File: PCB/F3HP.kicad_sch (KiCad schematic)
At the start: 108 parts, among them J1 L_In, J2 R_In, J3 AC_In, J4 Switch, J5 HPOut, K1 C93402, Q1 BC850C, Q10 BC860C, Q2 BC860C, Q3 BCP56, Q4 BC850C, Q5 BC860C, Q6 BCP56, Q7 BC850C, Q8 AO3400A, Q9 BC860C, U1 LT1965

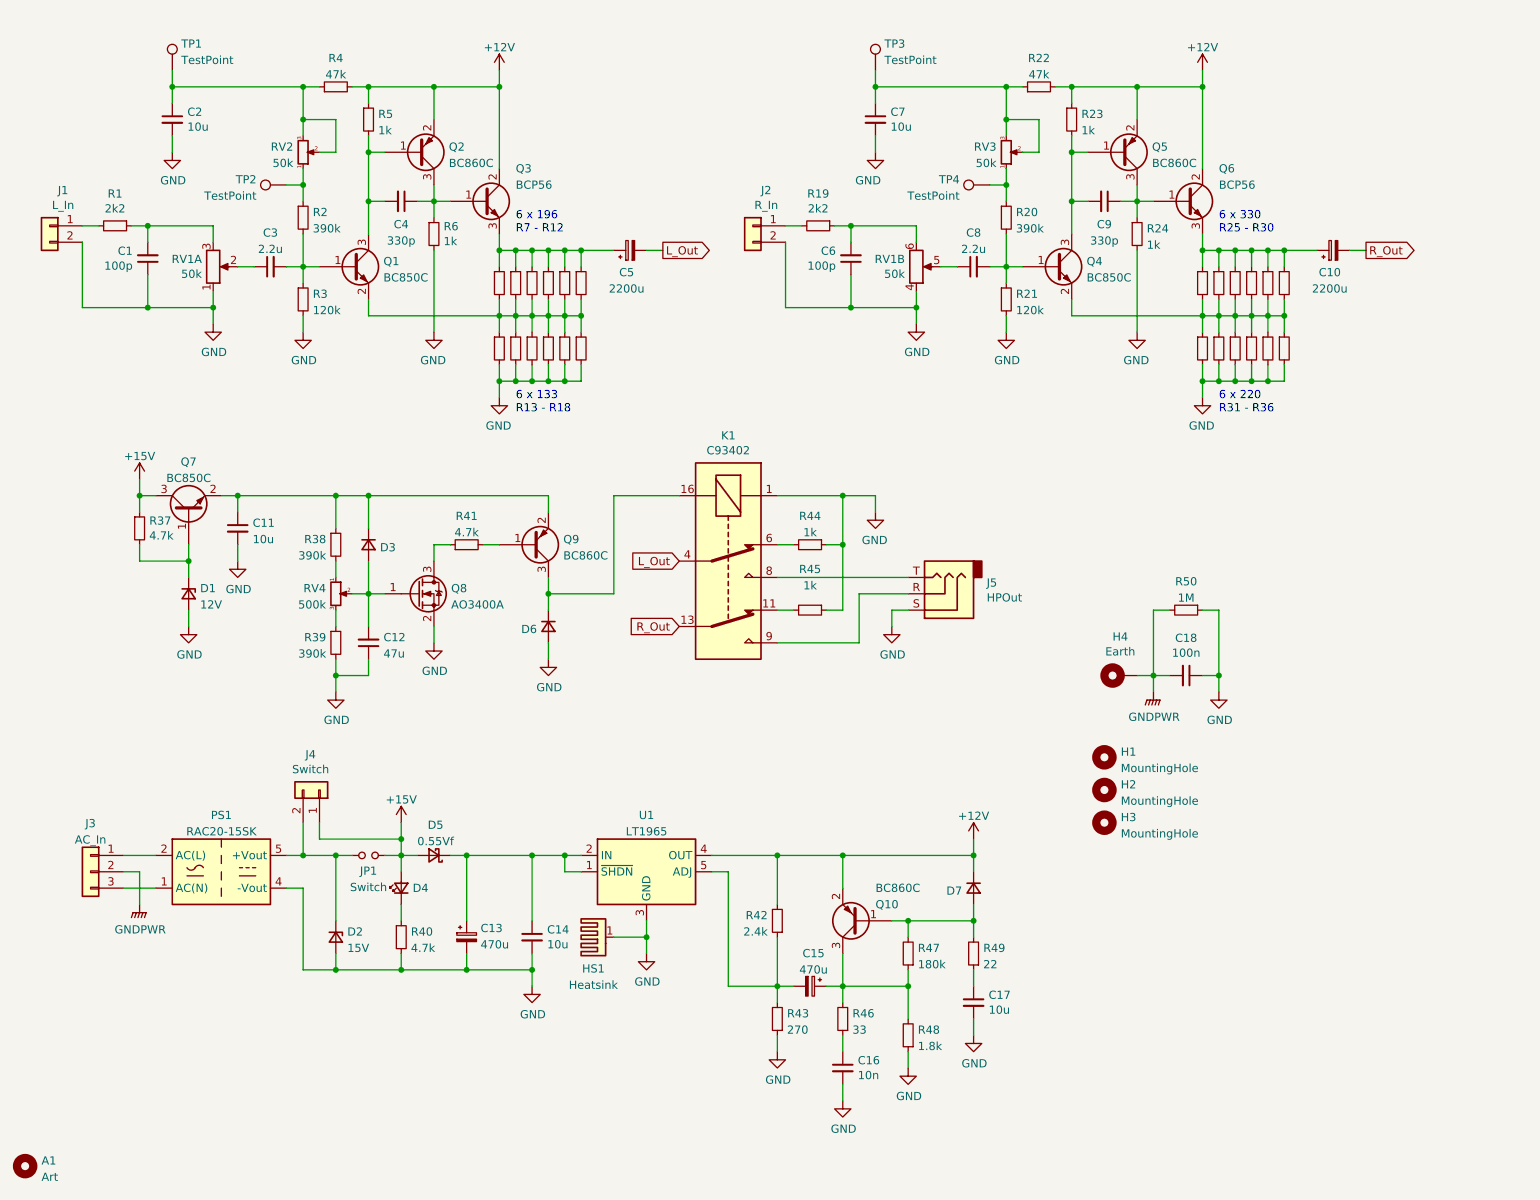
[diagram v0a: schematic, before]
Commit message: Better layout, better heatsinking
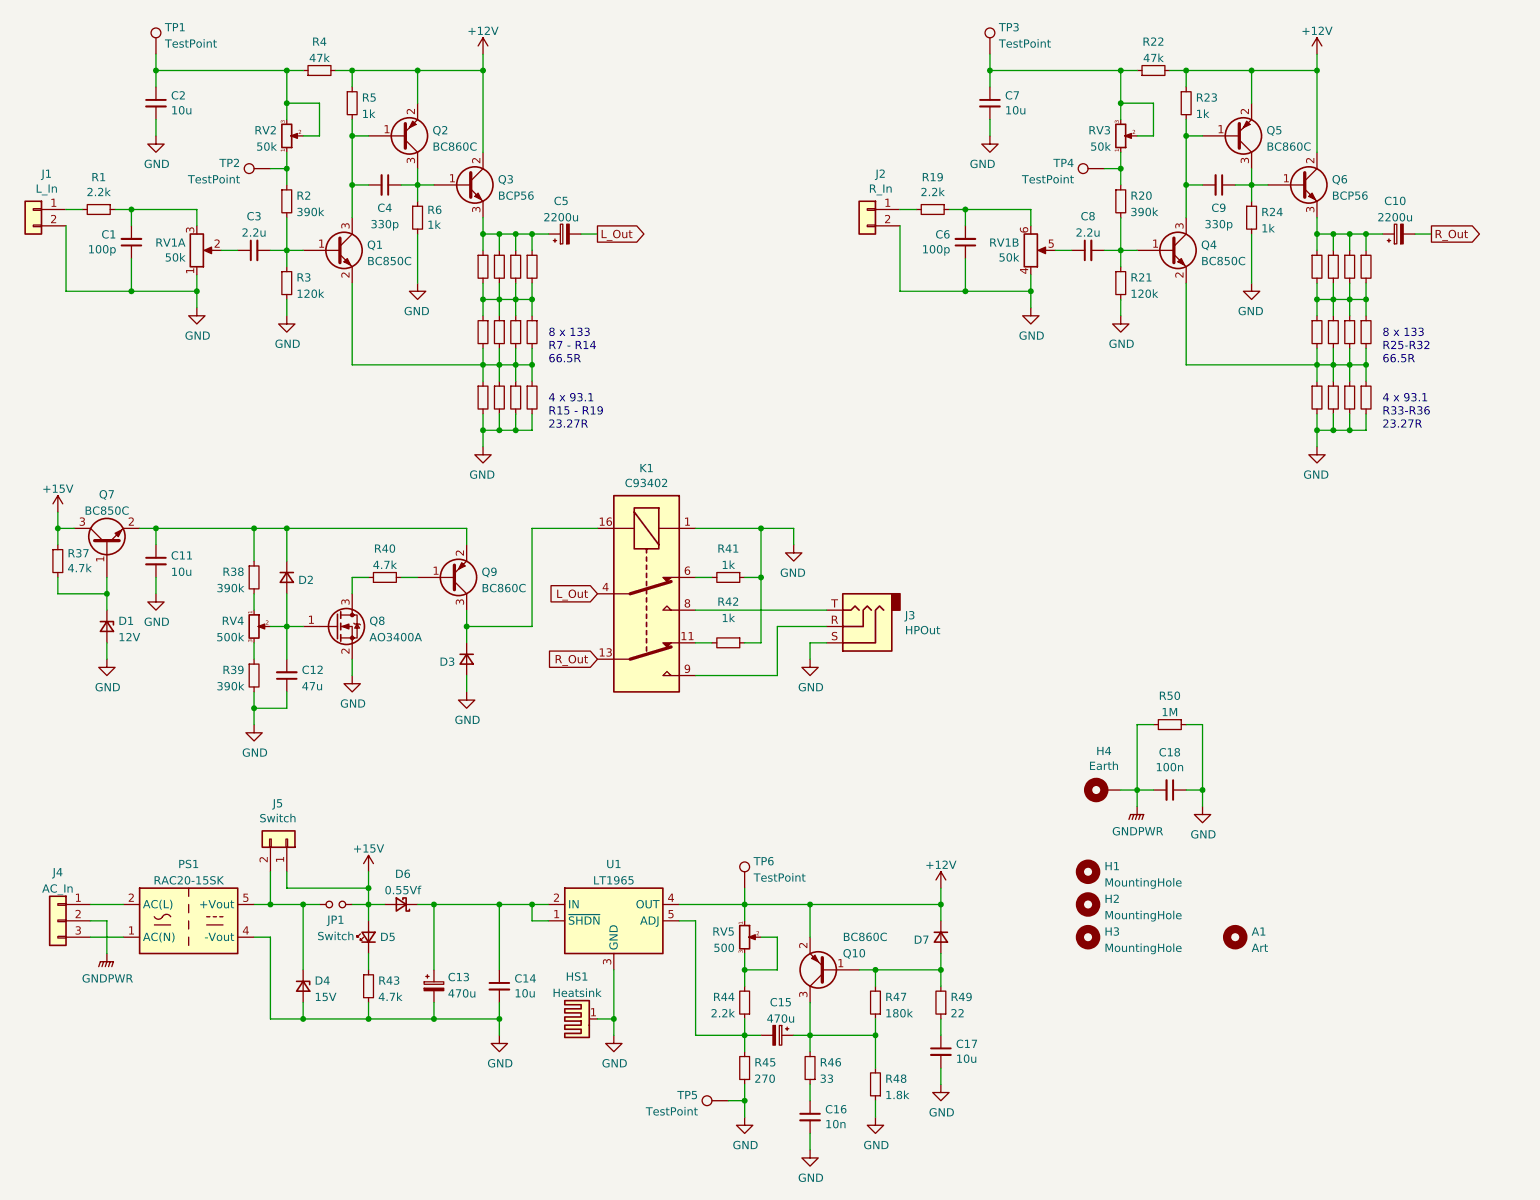
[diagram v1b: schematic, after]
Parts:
- removed R16, R17, R34, R35: 133, Resistor_SMD:R_1206_3216Metric, symbol Device:R_Small
- added R13, R14, R31, R32: 133, Resistor_SMD:R_1206_3216Metric, symbol Device:R_Small
- added RV5: 500, Potentiometer_THT:Potentiometer_Vishay_T73YP_Vertical, symbol Device:R_Potentiometer_Small
- added TP5, TP6: TestPoint, TestPoint:TestPoint_THTPad_D1.5mm_Drill0.7mm, symbol Connector:TestPoint
- Q3, Q6: LCSC part number C177012 -> (none); Part number BCP56TA -> (none)
- R1, R19: value 2k2 -> 2.2k
- R10: renamed from R11; value 196 -> 133; Part number RT1206FRE07196RL -> RT1206DRD07133RL
- R11: renamed from R9; value 196 -> 133; Part number RT1206FRE07196RL -> RT1206DRD07133RL
- R12, R25, R30, R7: value 196 -> 133; Part number RT1206FRE07196RL -> RT1206DRD07133RL
- R15: renamed from R13; value 133 -> 93.1; Part number RT1206DRD07133RL -> RT1206FRE0793R1L
- R16: renamed from R14; value 133 -> 93.1; Part number RT1206DRD07133RL -> RT1206FRE0793R1L
- R17: renamed from R15; value 133 -> 93.1; Part number RT1206DRD07133RL -> RT1206FRE0793R1L
- R18, R36: value 133 -> 93.1; Part number RT1206DRD07133RL -> RT1206FRE0793R1L
- R26: renamed from R28; value 196 -> 133; Part number RT1206FRE07196RL -> RT1206DRD07133RL
- R27: renamed from R26; value 196 -> 133; Part number RT1206FRE07196RL -> RT1206DRD07133RL
- R28: renamed from R29; value 196 -> 133; Part number RT1206FRE07196RL -> RT1206DRD07133RL
- R29: renamed from R27; value 196 -> 133; Part number RT1206FRE07196RL -> RT1206DRD07133RL
- R33: renamed from R31; value 133 -> 93.1; Part number RT1206DRD07133RL -> RT1206FRE0793R1L
- R34: renamed from R32; value 133 -> 93.1; Part number RT1206DRD07133RL -> RT1206FRE0793R1L
- R35: renamed from R33; value 133 -> 93.1; Part number RT1206DRD07133RL -> RT1206FRE0793R1L
- R44: renamed from R42; value 2.4k -> 2.2k; LCSC part number C784582 -> C706068; Part number RT0603BRE072K4L -> RT0603DRE072K2L
- R8: renamed from R10; value 196 -> 133; Part number RT1206FRE07196RL -> RT1206DRD07133RL
- R9: renamed from R8; value 196 -> 133; Part number RT1206FRE07196RL -> RT1206DRD07133RL
- RV2, RV3: LCSC part number C83686 -> C780226; Part number 3296W-1-503LF -> 3266W-1-503LF
- renumbered D3 to D2, D6 to D3, D2 to D4, D4 to D5, D5 to D6, J5 to J3, J3 to J4, J4 to J5, R41 to R40, R44 to R41, R45 to R42, R40 to R43, R43 to R45
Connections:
- net +12V: now also RV5.1, TP6.1; no longer R44.2
- net GND: now also TP5.1
- net at C5.1, Q3.3 (E), R11.1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: now also R13.1; no longer R10.1, R12.1, R8.1
- net at Q1.2 (E), R10.2, R12.2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: now also R14.2; no longer R11.2, R7.2, R9.2
- net at Q4.2 (E), R26.2, R28.2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: now also R32.2; no longer R25.2, R27.2, R29.2
- net at C10.1, Q6.3 (E), R25.1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: now also R31.1; no longer R26.1, R28.1, R30.1
- new net: R10.1, R11.2, R12.1, R13.2, R14.1, R7.2, R8.1, R9.2
- new net: R25.2, R26.1, R27.2, R28.1, R29.2, R30.1, R31.2, R32.1
- new net: R44.2, RV5.2, RV5.3
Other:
- note added: "4 x 93.1 R15 - R19 23.27R"
- note added: "4 x 93.1 R33-R36 23.27R"
- note added: "8 x 133 R25-R32 66.5R"
- note added: "8 x 133 R7 - R14 66.5R"
- note removed: "6 x 133 R13 - R18"
- note removed: "6 x 196 R7 - R12"
- note removed: "6 x 220 R31 - R36"
- note removed: "6 x 330 R25 - R30"
- moved on the sheet: C1, C10, C11, C12, C13, C14, C15, C16, C17, C18, C2, C3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

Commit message: Updated component values and BOM
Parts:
- HS1: LCSC part number (none) -> N/A; Part number (none) -> 573300D00000G
- Q1, Q4, Q7: Part number BC850C,235 -> BC850C
- Q10, Q2, Q5, Q9: Part number BC860C,235 -> BC860C
- Q3, Q6: value BCP56 -> BCP56TA; LCSC part number (none) -> C177012; Part number (none) -> BCP56TA
- R22, R4: value 47k -> 39k; LCSC part number C326743 -> C705983; Part number RT0603BRE0747KL -> RT0603DRD0739RL
- R23, R5: value 1k -> 820; LCSC part number C706049 -> C723589; Part number RT0603DRE071KL -> RT0603DRD07820RL
- R24, R6: value 1k -> 1.2k; LCSC part number C706049 -> C723656; Part number RT0603DRE071KL -> RT0603DRD071K2L
- RV2, RV3: value 50k -> 5k
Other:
- moved on the sheet: C10, C5

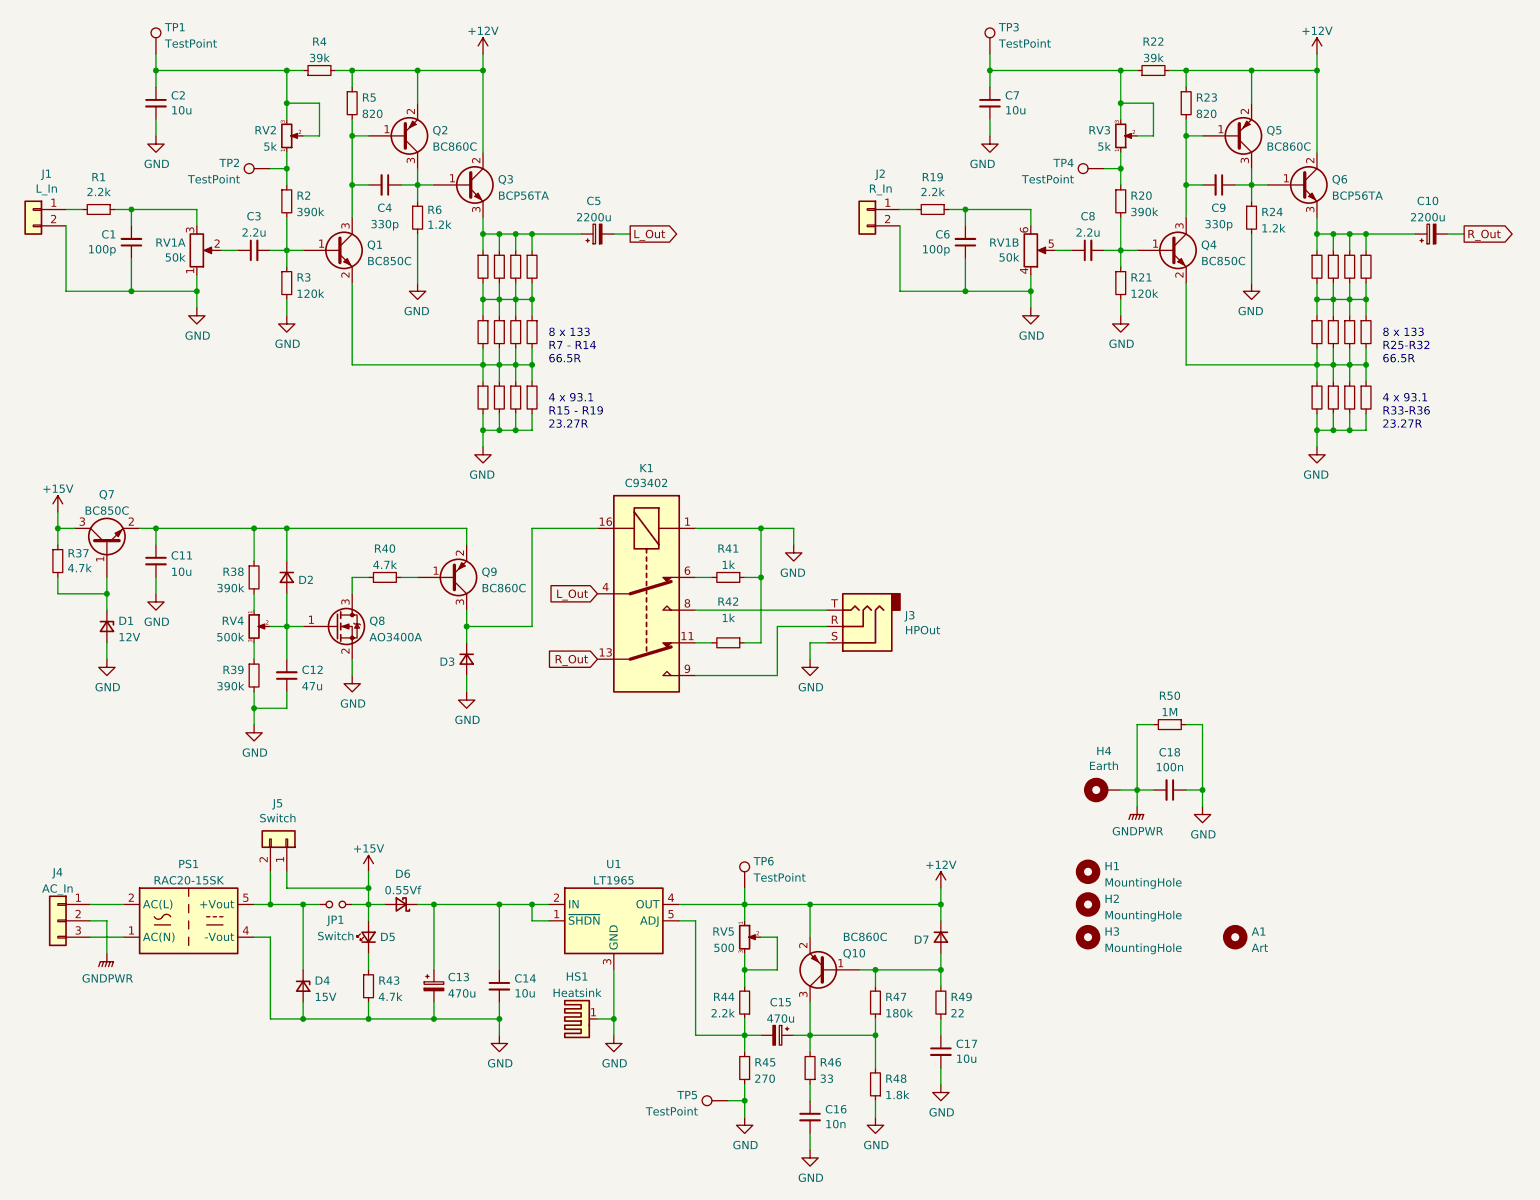
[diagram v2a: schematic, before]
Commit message: Swapped to TPS7A4701 LDO, better performance and less complicated PCB required
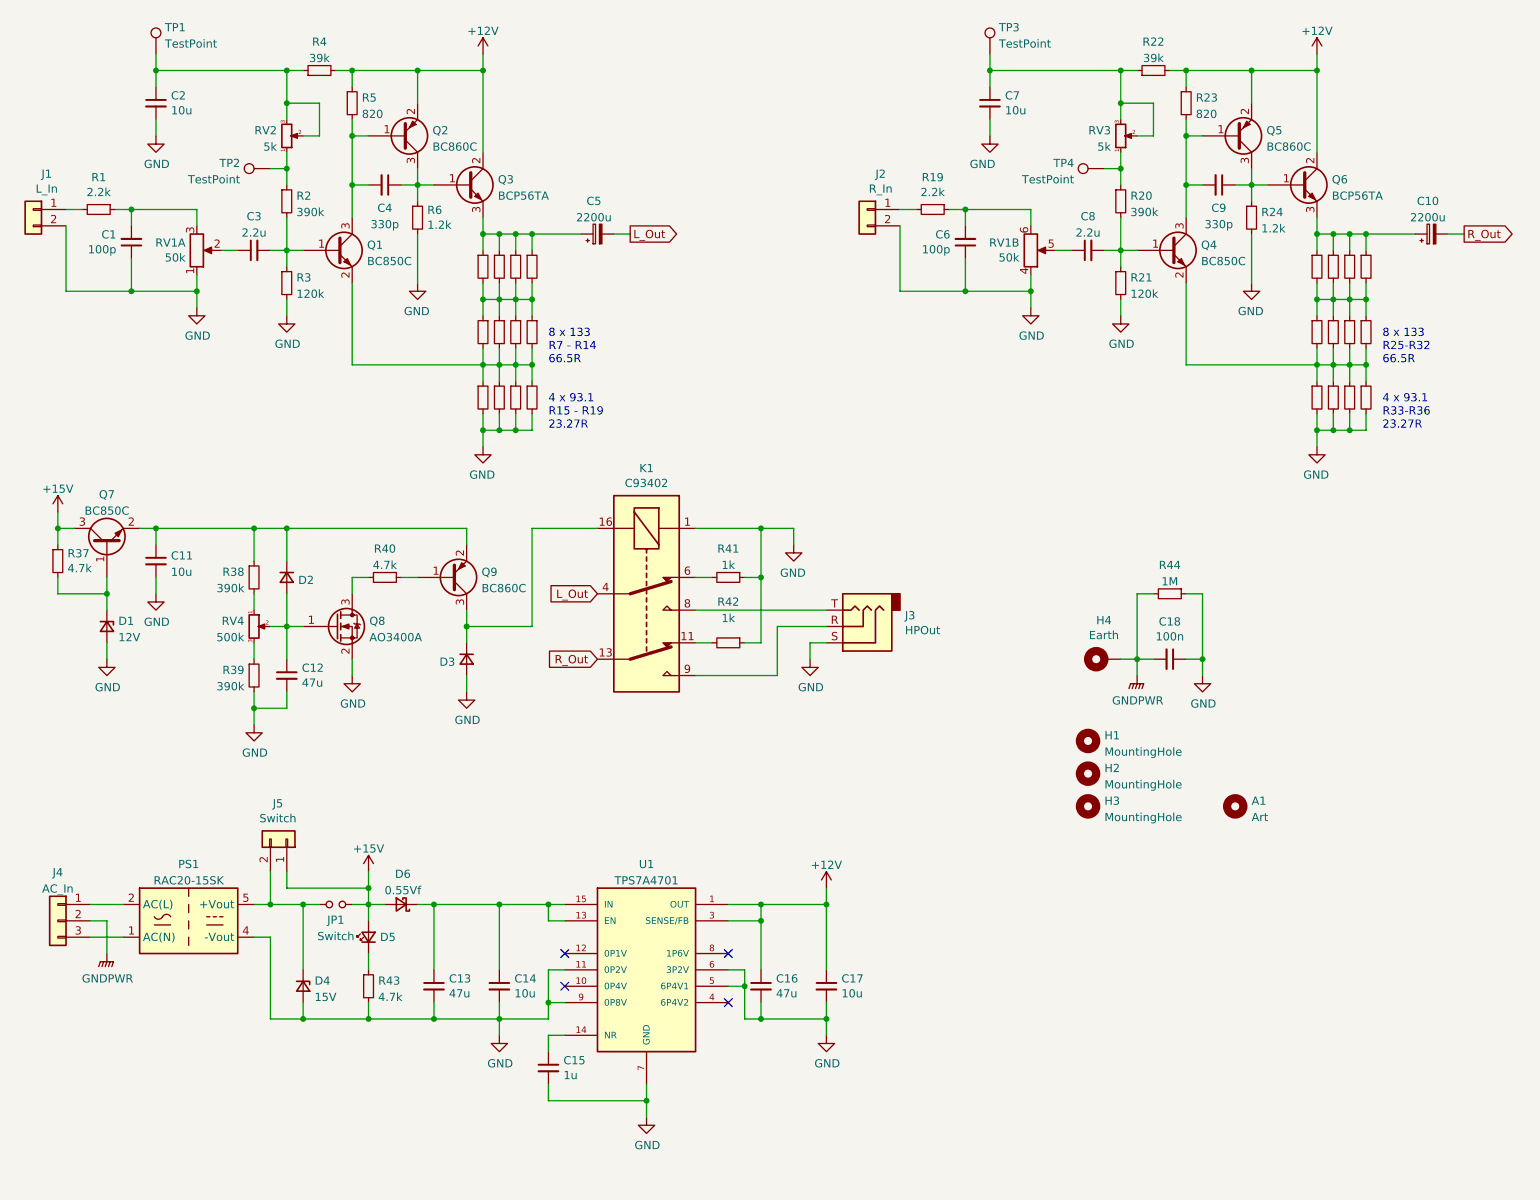
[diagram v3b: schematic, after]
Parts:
- removed C13, C15: 470u, Capacitor_SMD:CP_Elec_8x10.5, symbol Device:CP_Small
- removed D7: D, Diode_SMD:D_SOD-123, symbol Device:D_Small
- removed HS1: Heatsink, Heatsink:Heatsink_AAVID_573300D00010G_TO-263, symbol Mechanical:Heatsink_Pad
- removed Q10: BC860C, Package_TO_SOT_SMD:SOT-23, symbol Transistor_BJT:BC857
- removed R44: 2.2k, Resistor_SMD:R_0603_1608Metric, symbol Device:R_Small
- removed R45: 270, Resistor_SMD:R_0603_1608Metric, symbol Device:R_Small
- removed R46: 33, Resistor_SMD:R_0603_1608Metric, symbol Device:R_Small
- removed R47: 180k, Resistor_SMD:R_0603_1608Metric, symbol Device:R_Small
- removed R48: 1.8k, Resistor_SMD:R_0603_1608Metric, symbol Device:R_Small
- removed R49: 22, Resistor_SMD:R_0603_1608Metric, symbol Device:R_Small
- removed RV5: 500, Potentiometer_THT:Potentiometer_Vishay_T73YP_Vertical, symbol Device:R_Potentiometer_Small
- removed TP5, TP6: TestPoint, TestPoint:TestPoint_THTPad_D1.5mm_Drill0.7mm, symbol Connector:TestPoint
- removed U1: LT1965, Package_TO_SOT_SMD:TO-263-5_TabPin3, symbol Regulator_Linear:LT1963EQ
- added C13: 47u, Capacitor_SMD:C_1206_3216Metric, symbol Device:C_Small
- added C15: 1u, Capacitor_SMD:C_0603_1608Metric, symbol Device:C_Small
- added U1: TPS7A4701, Package_DFN_QFN:QFN-20-1EP_5x5mm_P0.65mm_EP3.35x3.35mm, symbol F3HP:TPS7A4701RGWR
- C12: footprint Capacitor_THT:C_Radial_D8.0mm_H11.5mm_P3.50mm -> Capacitor_SMD:C_1206_3216Metric; LCSC part number C1669286 -> C385907; Part number UES1C470MPM -> EMK316BBJ476ML-T
- C16: value 10n -> 47u; footprint Capacitor_SMD:C_0603_1608Metric -> Capacitor_SMD:C_1206_3216Metric; LCSC part number C1589 -> C385907; Part number CL10B103KB8NNNC -> EMK316BBJ476ML-T
- renumbered R50 to R44
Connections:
- net +12V: now also C16.1, C17.1, U1.1 (OUT), U1.20 (OUT), U1.3 (SENSE/FB)
- net GND: now also C12.2, C13.2, C15.2, U1.11 (0P2V), U1.17 (NC), U1.18 (NC), U1.19 (NC), U1.2 (NC), U1.21 (GND), U1.5 (6P4V1), U1.6 (3P2V), U1.7 (GND), U1.9 (0P8V); no longer C12.1
- net at D2.2 (A), Q8.1 (G), RV4.2: now also C12.1; no longer C12.2
- net at C14.1, D6.1 (K): now also C13.1, U1.13 (EN), U1.15 (IN), U1.16 (IN)
- new net: C15.1, U1.14 (NR)
- no-connect marks 0 -> 4
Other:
- moved on the sheet: A1, C18, H1, H2, H3, H4, R44

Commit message: Added back LC filter after ACDC converter
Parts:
- added C14: 470u, Capacitor_SMD:CP_Elec_8x10.5, symbol Device:C_Polarized_Small
- added L1: 100u, Inductor_SMD:L_TDK_SLF7032, symbol Device:L_Small
- added R44, R45: 1, Resistor_SMD:R_1206_3216Metric, symbol Device:R_Small
- renumbered C13 to C15, C14 to C16, C15 to C17, C16 to C18, C17 to C19, C18 to C20, R44 to R46
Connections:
- net GND: now also C14.2
- net at C15.1, C16.1, U1.13 (EN)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: now also C14.1, L1.2; no longer D6.1 (K)
- new net: D6.1 (K), R44.1, R45.1
- new net: L1.1, R44.2, R45.2
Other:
- moved on the sheet: C15, C16, C17, C18, C19, U1
